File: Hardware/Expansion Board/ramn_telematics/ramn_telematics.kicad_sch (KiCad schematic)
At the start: 43 parts, among them IC1 ESP32-S3-WROOM-1-N8, IC2 SGM2212-3.3XKC3G_TR, J1 Main RAMN Connection, J2 105164-0001, J4 105164-0001, Q1 L8050QLT1G, Q2 L8050QLT1G, U1 CP2102N-Axx-xQFN28

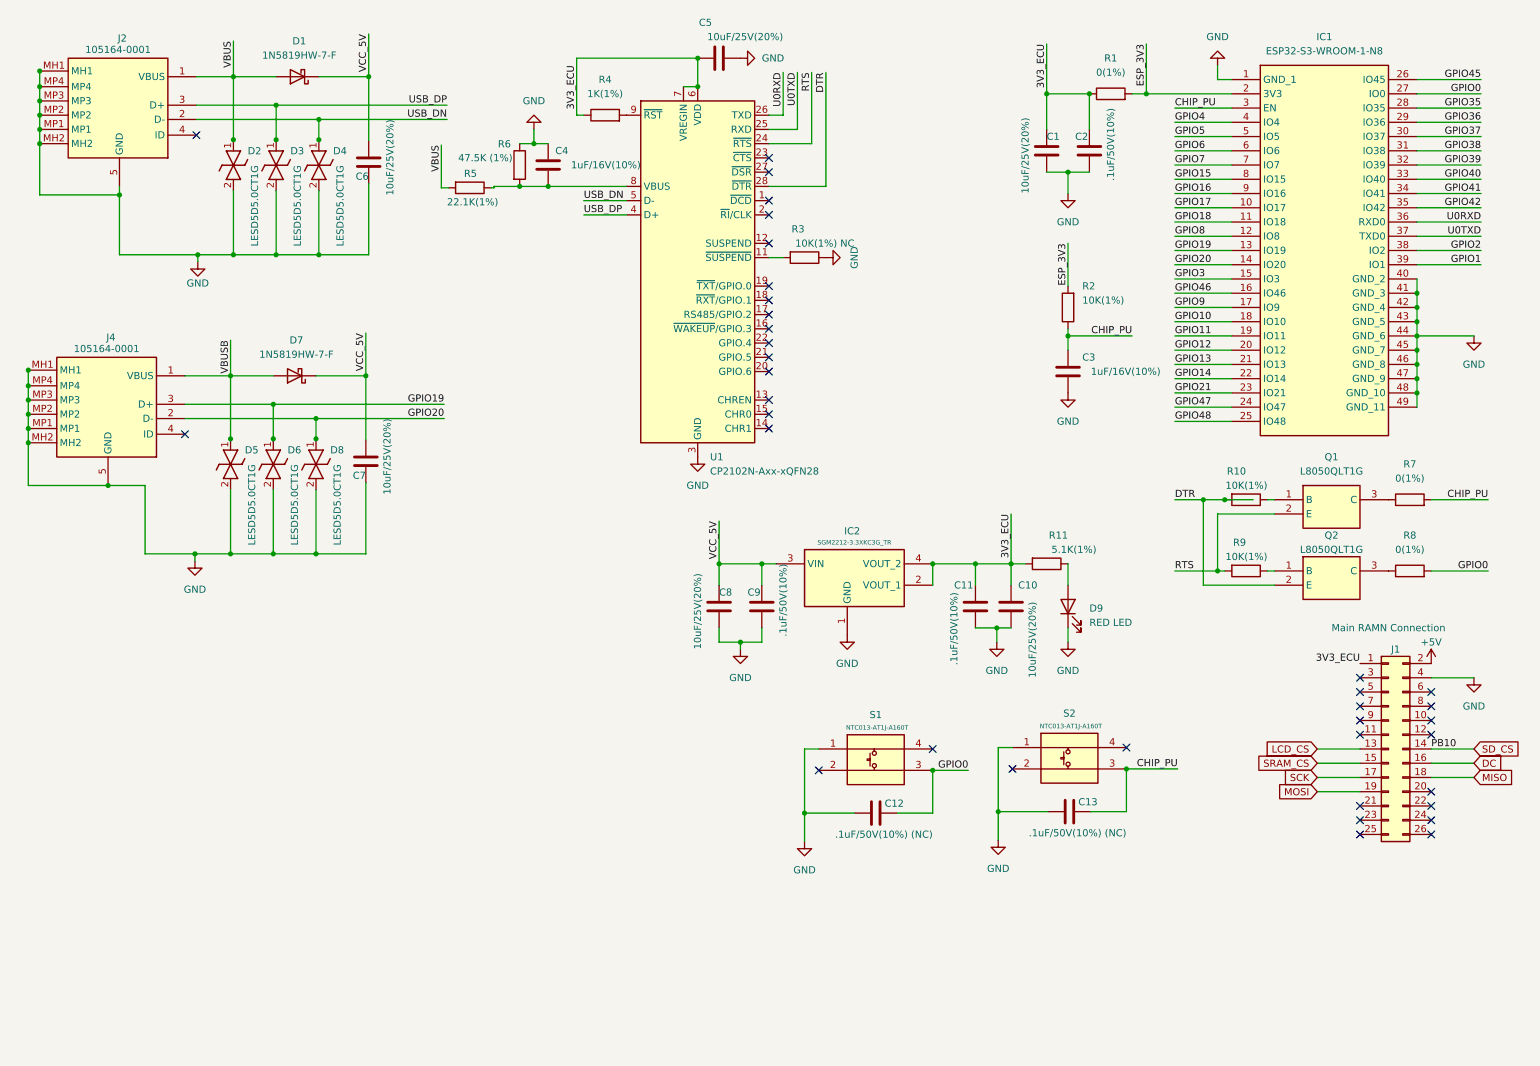
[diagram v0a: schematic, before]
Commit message: More Board Revisions
Trying to update to components that are available in JLCPCB
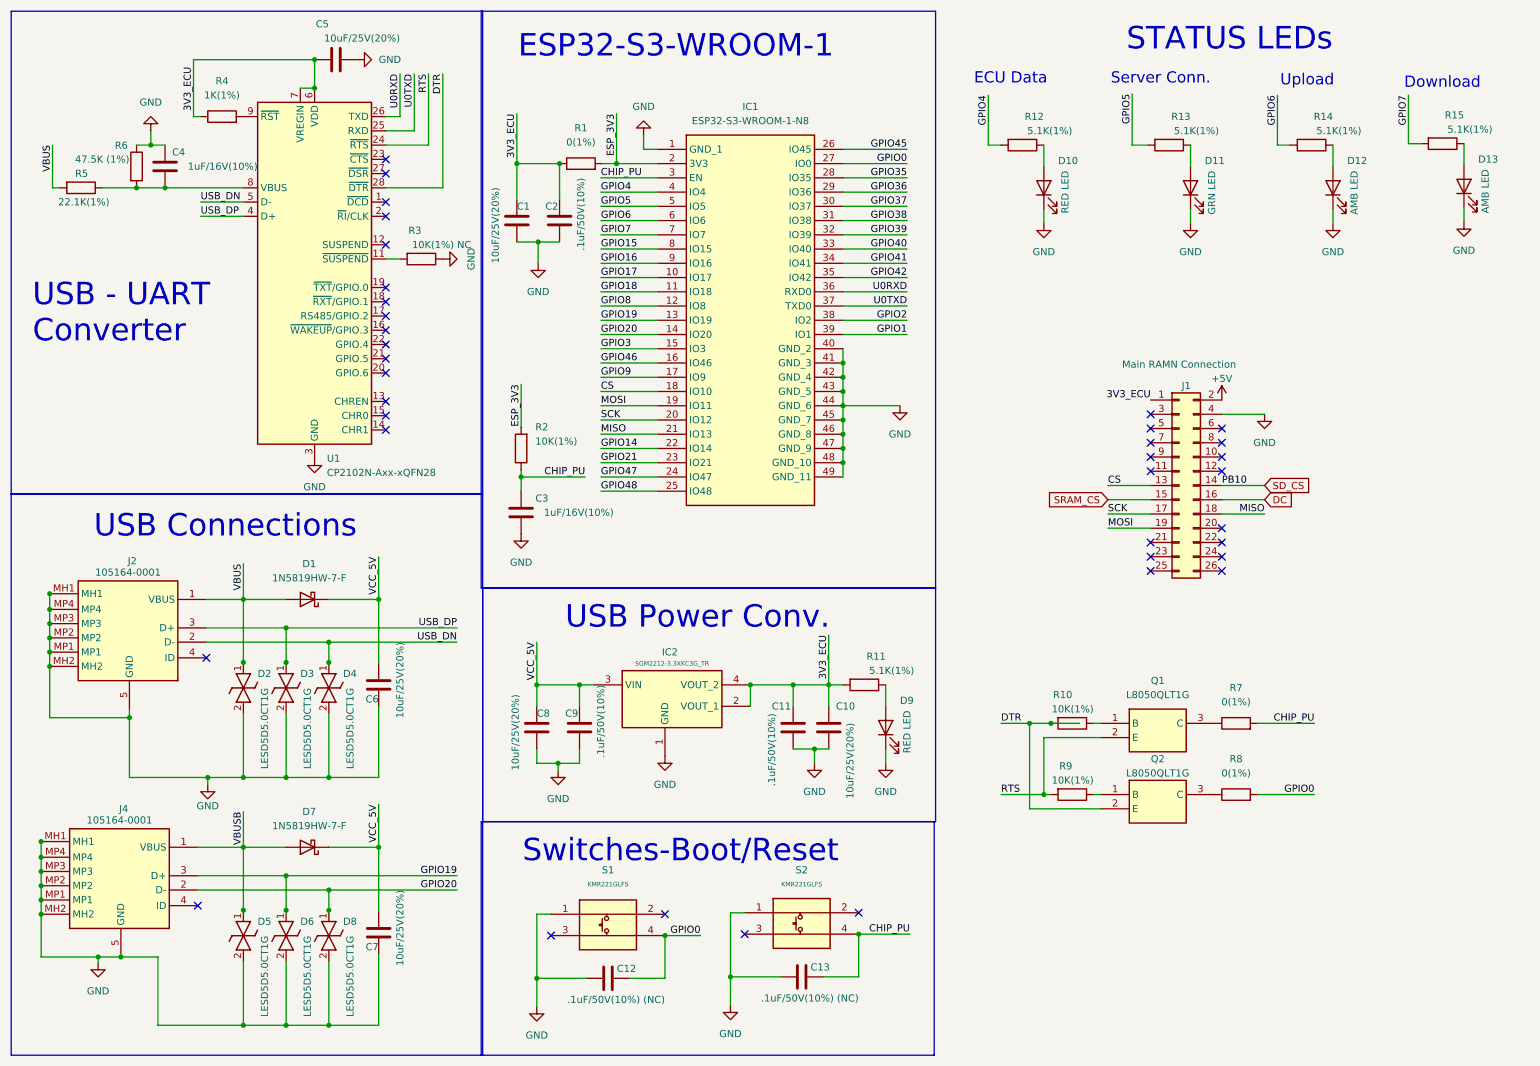
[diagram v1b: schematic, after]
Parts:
- removed S1, S2: NTC013-AT1J-A160T, SamacSys_Parts:NTC013AT1JA160T, symbol SamacSys_Parts:NTC013-AT1J-A160T
- added D10: RED LED, LED_SMD:LED_0603_1608Metric, symbol Device:LED
- added D11: GRN LED, LED_SMD:LED_0603_1608Metric, symbol Device:LED
- added D12, D13: AMB LED, LED_SMD:LED_0603_1608Metric, symbol Device:LED
- added R12, R13, R14, R15: 5.1K(1%), Resistor_SMD:R_0402_1005Metric, symbol Device:R
- added S1, S2: KMR221GLFS, Library:KMR221GLFS_PUSH_SMD_SWITCH_2.8mmx1.9mm, symbol SamacSys_Parts:KMR221GLFS
- C1, C10, C5, C8: footprint Capacitor_SMD:C_0402_1005Metric -> Capacitor_SMD:C_0603_1608Metric; JLCPCB (none) -> C76614
- C2, C3, C4: footprint Capacitor_SMD:C_0402_1005Metric -> Capacitor_SMD:C_0603_1608Metric; JLCPCB (none) -> C5673
- C6: footprint Capacitor_SMD:C_0402_1005Metric -> Capacitor_SMD:C_0603_1608Metric; JLCPCB# (none) -> C76614; MFR.PART# (none) -> C1608X5R1E106MT000E
- C7: footprint Capacitor_SMD:C_0402_1005Metric -> Capacitor_SMD:C_0603_1608Metric; JLCPCB# (none) -> C76614; MFR PRT# (none) -> C1608X5R1E106MT000E
- D9: JLCPCB (none) -> C79636
- Q1, Q2: JLCPCB (none) -> C49581
- R11: JLCPCB (none) -> C72044
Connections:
- net GPIO11 is gone; now on net MOSI: IC1.19 (IO11)
- net GPIO12 is gone; now on net SCK: IC1.20 (IO12)
- net GPIO13 is gone; now on net MISO: IC1.21 (IO13)
- net LCD_CS is gone; now on net CS: J1.13 (Pin_13)
- net CHIP_PU: now also S2.4
- net GND: now also D10.1 (K), D11.1 (K), D12.1 (K), D13.1 (K), S1.1, S2.1
- net GPIO0: now also S1.4
- net GPIO4: now also R12.2
- net GPIO5: now also R13.2
- net GPIO6: now also R14.2
- net GPIO7: now also R15.2
- net GPIO10 renamed CS
- new net: D11.2 (A), R13.1
- new net: D12.2 (A), R14.1
- new net: D10.2 (A), R12.1
- new net: D13.2 (A), R15.1
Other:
- note added: "Download"
- note added: "ECU Data"
- note added: "ESP32-S3-WROOM-1"
- note added: "STATUS LEDs"
- note added: "Server Conn."
- note added: "Switches-Boot/Reset"
- note added: "USB - UART Converter"
- note added: "USB Connections"
- note added: "USB Power Conv."
- note added: "Upload"
- moved on the sheet: C1, C10, C11, C12, C13, C2, C3, C4, C5, C6, C7, C8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
